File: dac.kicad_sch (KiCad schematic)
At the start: 63 parts, among them J16 3.5mm_Jack, J9 3.5mm_Jack, Q2 FMMT591, Q3 FMMT491, Q4 FMMT491, Q5 FMMT591, U1 CJC4334H, U9 OPA1612AxD

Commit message: Updated errors
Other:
- note added: "Disconnect this if you want to use more than +5V fdr the analog voltage input."
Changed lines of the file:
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@@
 	(generator_version "10.0")
 	(paper "A")
+	(text "Disconnect this if you want to use more than +5V\nfdr the analog voltage input."
+		(exclude_from_sim no)
+		(at 221.742 22.098 0)
+		(effects
+			(font
+				(size 1.27 1.27)
+			)
+		)
+	)
 	(text "D6 needs to be close to Q4\nand D7 needs to be close to Q5.  \nSimilarly, Q3 by D4 and Q2 by D5."
 		(exclude_from_sim no)
@@
 	)
 	(junction
+		(at 204.47 85.09)
+		(diameter 0)
+		(color 0 0 0 0)
+	)
+	(junction
 		(at 157.48 114.3)
 		(diameter 0)
@@
 	)
 	(junction
-		(at 203.2 85.09)
+		(at 82.55 59.69)
 		(diameter 0)
 		(color 0 0 0 0)
 	)
 	(junction
-		(at 82.55 59.69)
+		(at 204.47 62.23)
 		(diameter 0)
 		(color 0 0 0 0)
@@
 	)
 	(junction
-		(at 203.2 62.23)
-		(diameter 0)
-		(color 0 0 0 0)
-	)
-	(junction
 		(at 184.15 43.18)
 		(diameter 0)
@@
 	(wire
 		(pts
-			(xy 203.2 85.09) (xy 203.2 62.23)
+			(xy 204.47 85.09) (xy 208.28 85.09)
+		)
+		(stroke
+			(width 0)
+			(type default)
+		)
+	)
+	(wire
+		(pts
+			(xy 204.47 85.09) (xy 204.47 62.23)
 		)
 		(stroke
@@
 	(wire
 		(pts
-			(xy 165.1 85.09) (xy 203.2 85.09)
+			(xy 165.1 85.09) (xy 204.47 85.09)
 		)
 		(stroke
@@
 	(wire
 		(pts
-			(xy 203.2 62.23) (xy 199.39 62.23)
+			(xy 199.39 62.23) (xy 204.47 62.23)
 		)
 		(stroke
@@
 	(wire
 		(pts
-			(xy 203.2 85.09) (xy 208.28 85.09)
-		)
-		(stroke
-			(width 0)
-			(type default)
-		)
-	)
-	(wire
-		(pts
 			(xy 191.77 34.29) (xy 187.96 34.29)
 		)
@@
 	(symbol
 		(lib_id "Connector:TestPoint")
-		(at 203.2 62.23 270)
+		(at 204.47 62.23 270)
 		(unit 1)
 		(body_style 1)
@@
 		(dnp no)
 		(property "Reference" "TP8"
-			(at 209.55 62.23 90)
+			(at 210.82 62.23 90)
 			(hide yes)
 			(show_name no)
@@
 		)
 		(property "Value" "V_R"
-			(at 205.74 59.69 90)
+			(at 207.01 59.69 90)
 			(show_name no)
 			(do_not_autoplace no)
@@
 		)
 		(property "Footprint" "TestPoint:TestPoint_THTPad_D1.5mm_Drill0.7mm"
-			(at 203.2 67.31 0)
+			(at 204.47 67.31 0)
 			(hide yes)
 			(show_name no)
@@
 		)
 		(property "Datasheet" ""
-			(at 203.2 67.31 0)
+			(at 204.47 67.31 0)
 			(hide yes)
 			(show_name no)
@@
 		)
 		(property "Description" ""
-			(at 203.2 62.23 0)
+			(at 204.47 62.23 0)
 			(hide yes)
 			(show_name no)
@@
 		)
 		(property "JLCPCB #" ""
-			(at 203.2 62.23 0)
+			(at 204.47 62.23 0)
 			(hide yes)
 			(show_name no)

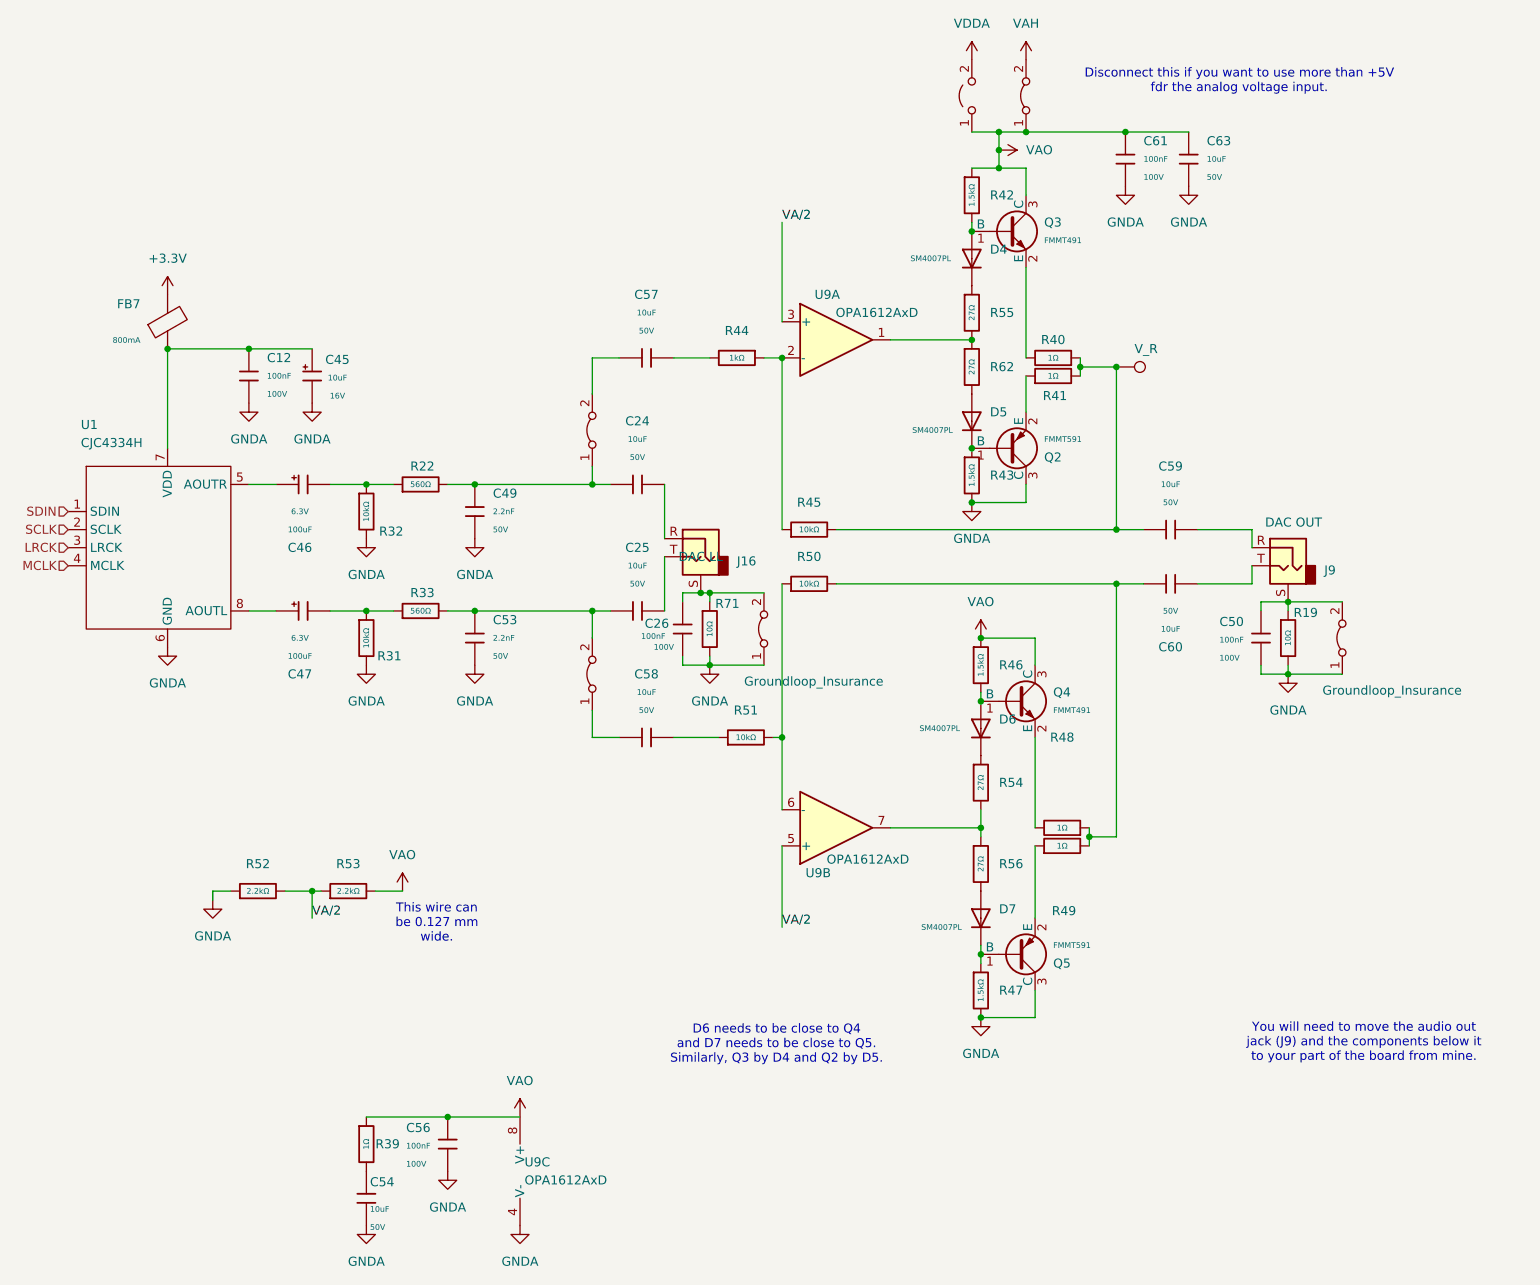
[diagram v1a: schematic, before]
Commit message: Starting a new branch for v0.2
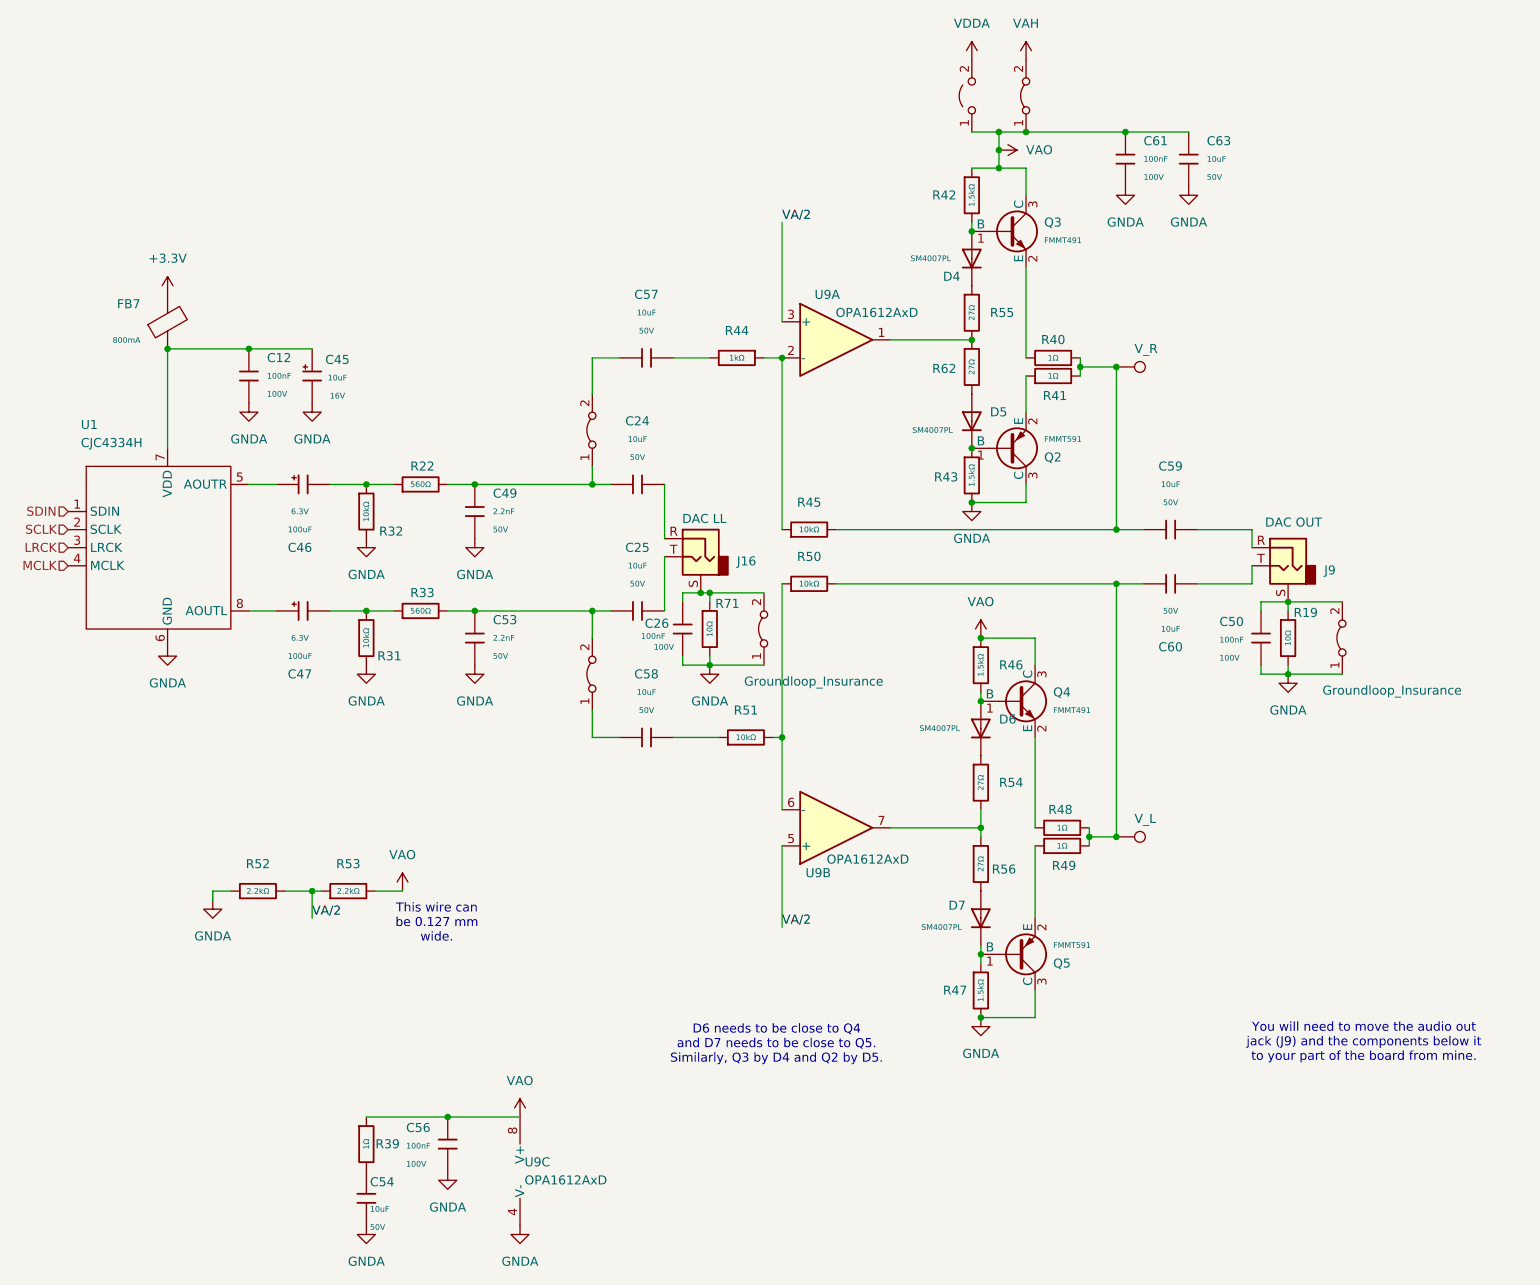
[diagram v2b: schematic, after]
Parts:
- added TP9: V_L, TestPoint:TestPoint_THTPad_D1.5mm_Drill0.7mm, symbol Connector:TestPoint
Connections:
- net at C60.1, R48.1, R49.2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: now also TP9.1
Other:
- note removed: "Disconnect this if you want to use more than +5V fdr the analog voltage input."
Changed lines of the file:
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@@
 	(generator_version "10.0")
 	(paper "A")
-	(text "Disconnect this if you want to use more than +5V\nfdr the analog voltage input."
-		(exclude_from_sim no)
-		(at 221.742 22.098 0)
-		(effects
-			(font
-				(size 1.27 1.27)
-			)
-		)
-	)
 	(text "D6 needs to be close to Q4\nand D7 needs to be close to Q5.  \nSimilarly, Q3 by D4 and Q2 by D5."
 		(exclude_from_sim no)
@@
 	)
 	(junction
+		(at 204.47 128.27)
+		(diameter 0)
+		(color 0 0 0 0)
+	)
+	(junction
 		(at 187.96 29.21)
 		(diameter 0)
@@
 		(dnp no)
 		(property "Reference" "R49"
-			(at 197.104 138.684 90)
+			(at 197.104 132.334 90)
 			(show_name no)
 			(do_not_autoplace no)
@@
 		(in_pos_files yes)
 		(dnp no)
-		(fields_autoplaced yes)
 		(property "Reference" "R43"
-			(at 186.69 77.4699 0)
+			(at 178.816 77.724 0)
 			(show_name no)
 			(do_not_autoplace no)
@@
 		)
 		(property "Description" "DAC LL"
-			(at 146.05 88.9 0)
+			(at 146.558 83.566 0)
 			(show_name no)
 			(do_not_autoplace no)
@@
 		(dnp no)
 		(property "Reference" "D7"
-			(at 187.96 138.4299 0)
+			(at 180.848 137.922 0)
 			(show_name no)
 			(do_not_autoplace no)
@@
 	)
 	(symbol
+		(lib_id "Connector:TestPoint")
+		(at 204.47 128.27 270)
+		(unit 1)
+		(body_style 1)
+		(exclude_from_sim no)
+		(in_bom yes)
+		(on_board yes)
+		(in_pos_files yes)
+		(dnp no)
+		(property "Reference" "TP9"
+			(at 210.82 128.27 90)
+			(hide yes)
+			(show_name no)
+			(do_not_autoplace no)
+			(effects
+				(font
+					(size 1.27 1.27)
+				)
+				(justify left)
+			)
+		)
+		(property "Value" "V_L"
+			(at 207.01 125.73 90)
+			(show_name no)
+			(do_not_autoplace no)
+			(effects
+				(font
+					(size 1.27 1.27)
+				)
+				(justify left)
+			)
+		)
+		(property "Footprint" "TestPoint:TestPoint_THTPad_D1.5mm_Drill0.7mm"
+			(at 204.47 133.35 0)
+			(hide yes)
+			(show_name no)
+			(do_not_autoplace no)
+			(effects
+				(font
+					(size 1.27 1.27)
+				)
+			)
+		)
+		(property "Datasheet" ""
+			(at 204.47 133.35 0)
+			(hide yes)
+			(show_name no)
+			(do_not_autoplace no)
+			(effects
+				(font
+					(size 1.27 1.27)
+				)
+			)
+		)
+		(property "Description" ""
+			(at 204.47 128.27 0)
+			(hide yes)
+			(show_name no)
+			(do_not_autoplace no)
+			(effects
+				(font
+					(size 1.27 1.27)
+				)
+			)
+		)
+		(property "JLCPCB #" ""
+			(at 204.47 128.27 0)
+			(hide yes)
+			(show_name no)
+			(do_not_autoplace no)
+			(effects
+				(font
+					(size 1.27 1.27)
+				)
+			)
+		)
+		(pin "1"
+		)
+		(instances
+			(project "Intro-to-CAD-2026"
+				(path "/c12dc015-e6cb-468c-8de4-269c3106de0e/483699fc-423f-4ea3-8184-654c25c5d0a3"
+					(reference "TP9")
+					(unit 1)
+				)
+			)
+		)
+	)
+	(symbol
 		(lib_id "PCM_JLCPCB-Capacitors:0805,2.2nF")
 		(at 114.3 100.33 0)
@@
 		(in_pos_files yes)
 		(dnp no)
-		(fields_autoplaced yes)
 		(property "Reference" "R62"
-			(at 186.69 62.2299 0)
+			(at 178.562 62.484 0)
 			(show_name no)
 			(do_not_autoplace no)
@@
 		(in_pos_files yes)
 		(dnp no)
-		(fields_autoplaced yes)
 		(property "Reference" "R47"
-			(at 187.96 149.8599 0)
+			(at 180.086 149.86 0)
 			(show_name no)
 			(do_not_autoplace no)
@@
 		(in_pos_files yes)
 		(dnp no)
-		(fields_autoplaced yes)
 		(property "Reference" "R56"
-			(at 187.96 132.0799 0)
+			(at 186.944 132.842 0)
 			(show_name no)
 			(do_not_autoplace no)
@@
 		(dnp no)
 		(property "Reference" "R48"
-			(at 196.85 114.3 90)
+			(at 196.596 124.46 90)
 			(show_name no)
 			(do_not_autoplace no)
@@
 		(in_pos_files yes)
 		(dnp no)
-		(fields_autoplaced yes)
 		(property "Reference" "R42"
-			(at 186.69 38.0999 0)
+			(at 178.562 38.1 0)
 			(show_name no)
 			(do_not_autoplace no)
@@
 		(dnp no)
 		(property "Reference" "D4"
-			(at 186.69 45.7199 0)
+			(at 180.086 49.53 0)
 			(show_name no)
 			(do_not_autoplace no)

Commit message: Saved schematic
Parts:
- added C95, C96: 100uF, PCM_JLCPCB:C_CASE-B-3528-21(mm), symbol PCM_JLCPCB-Capacitors:CASE-B-3528-21(mm),100uF
- added C97, C98: 100nF, PCM_JLCPCB:C_0805, symbol PCM_JLCPCB-Capacitors:0805,100nF
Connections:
- net GNDA: now also C95.2, C97.1
- net VAO: now also C96.1, C98.2
- net VA/2: now also C95.1, C96.2, C97.2, C98.1
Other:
- note removed: "This wire can be 0.127 mm wide."

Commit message: Placed the second ADC
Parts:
- C12, C26, C49, C50, C53, C54, C56, C61, C97, C98: Manufacturer Samsung Electro-Mechanics -> (none)
- C24, C25, C57, C58, C59, C60, C63: Manufacturer Murata Electronics -> (none)
- C45, C46, C47, C95, C96: Manufacturer AVX -> (none)
- D4, D5, D6, D7: Manufacturer MDD（Microdiode Electronics） -> (none)
- FB7: Manufacturer Sunlord -> (none)
- Q2, Q3, Q4, Q5: Manufacturer hongjiacheng -> (none)
- R19, R22, R31, R32, R33, R39, R40, R41, R42, R43, R44, R45, R46, R47, R48, R49, R50, R51, R52, R53, R54, R55, R56, R62, R71: Manufacturer UNI-ROYAL(Uniroyal Elec) -> (none)
- TP8, TP9: footprint TestPoint:TestPoint_THTPad_D1.5mm_Drill0.7mm -> TestPoint:TestPoint_THTPad_D2.0mm_Drill1.0mm

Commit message: More routing
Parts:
- TP8, TP9: footprint TestPoint:TestPoint_THTPad_D2.0mm_Drill1.0mm -> TP_Label:TestPoint_THTPad_D2.0mm_Drill1.0mm
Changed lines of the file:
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@@
 			)
 		)
-		(property "Footprint" "TestPoint:TestPoint_THTPad_D2.0mm_Drill1.0mm"
+		(property "Footprint" "TP_Label:TestPoint_THTPad_D2.0mm_Drill1.0mm"
 			(at 204.47 133.35 0)
 			(hide yes)
@@
 			)
 		)
-		(property "Footprint" "TestPoint:TestPoint_THTPad_D2.0mm_Drill1.0mm"
+		(property "Footprint" "TP_Label:TestPoint_THTPad_D2.0mm_Drill1.0mm"
 			(at 204.47 67.31 0)
 			(hide yes)
